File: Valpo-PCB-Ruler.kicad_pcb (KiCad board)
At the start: 2 copper layers, 159 x 38.1 mm, 40 parts, among them SW1 SW_Push, SW2 SW_Push, SW3 SW_Push, U2 USB_Board, U3 ATtiny85-20SU

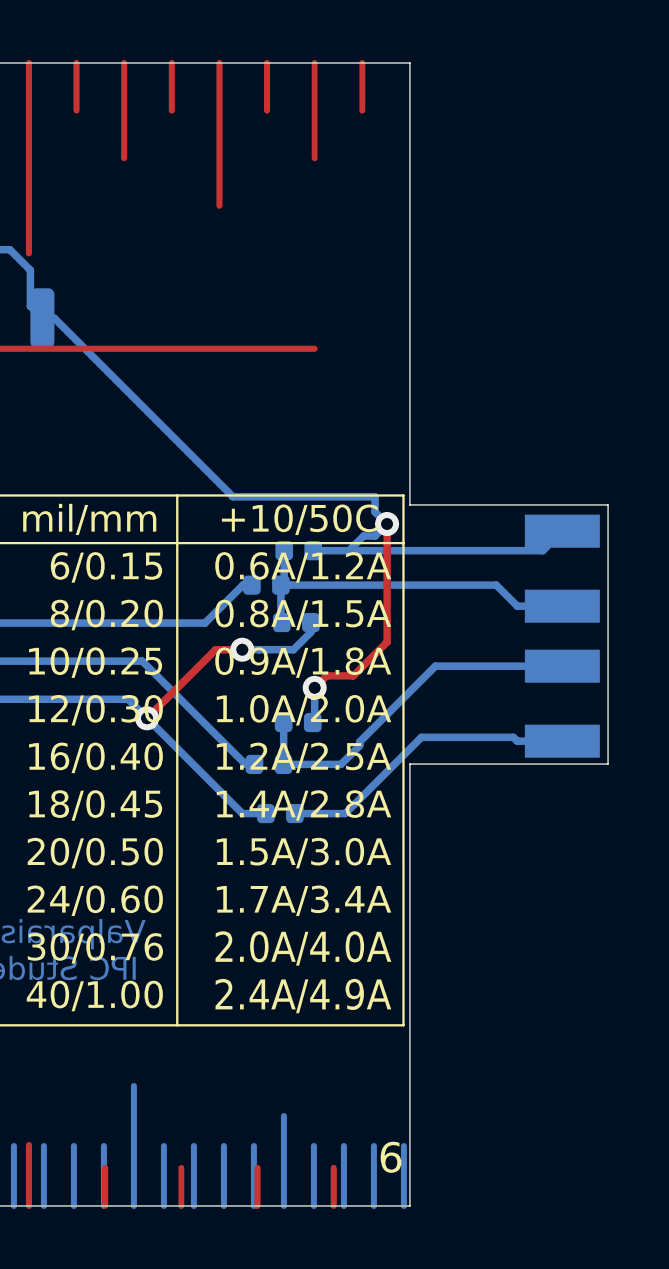
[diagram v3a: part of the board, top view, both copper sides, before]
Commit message: Reduce USB size
Brought the sides of the USB down to more closely fit the width of the pads.
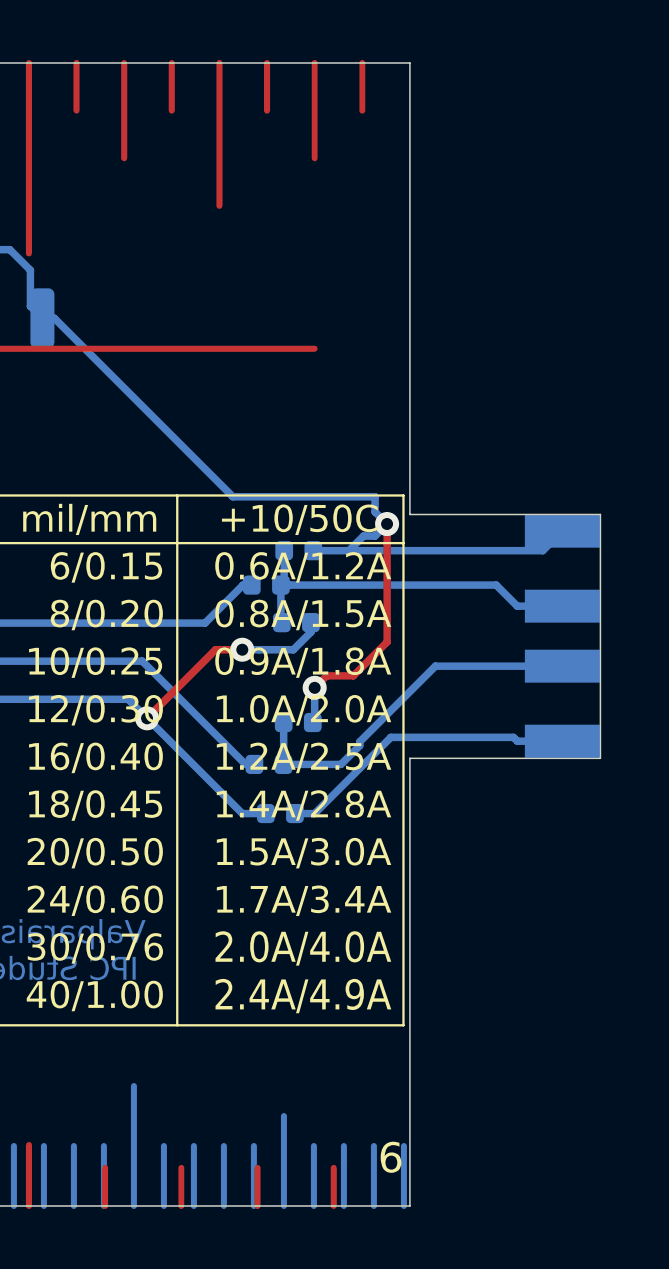
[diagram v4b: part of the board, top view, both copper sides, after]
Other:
- board size 159 x 38.1 mm -> 158.8 x 38.1 mm
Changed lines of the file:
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@@
     (tags diode)
     (attr smd)
-    (fp_text reference D2 (at 2.055 0) (layer B.SilkS)
+    (fp_text reference D2 (at -2.159 -0.254) (layer B.SilkS)
       (effects (font (size 1 1) (thickness 0.15)) (justify mirror))
     )
@@
     (effects (font (size 1 1) (thickness 0.15)) (justify left mirror))
   )
-  (gr_line (start 203.2 86.868) (end 209.804 86.868) (layer Edge.Cuts) (width 0.05))
-  (gr_line (start 203.2 78.232) (end 209.804 78.232) (layer Edge.Cuts) (width 0.05))
-  (gr_line (start 203.2 63.5) (end 203.2 78.232) (layer Edge.Cuts) (width 0.05))
-  (gr_line (start 209.804 78.232) (end 209.804 86.868) (layer Edge.Cuts) (width 0.05))
+  (gr_line (start 203.2 86.6775) (end 209.55 86.6775) (layer Edge.Cuts) (width 0.05))
+  (gr_line (start 203.2 78.5495) (end 209.55 78.5495) (layer Edge.Cuts) (width 0.05))
+  (gr_line (start 203.2 63.5) (end 203.2 78.5495) (layer Edge.Cuts) (width 0.05))
+  (gr_line (start 209.55 78.5495) (end 209.55 86.6775) (layer Edge.Cuts) (width 0.05))
   (gr_text -31 (at 90.3224 66.8147) (layer B.SilkS)
     (effects (font (size 0.75 0.75) (thickness 0.15)) (justify mirror))
@@
     (effects (font (size 3.048 3.048) (thickness 0.15)))
   )
-  (gr_line (start 203.2 86.868) (end 203.2 101.6) (layer Edge.Cuts) (width 0.05))
-  (via (at 197.612 83.058) (size 0.8) (drill 0.4) (layers F.Cu B.Cu) (net 2))
+  (gr_line (start 203.2 86.6775) (end 203.2 101.6) (layer Edge.Cuts) (width 0.05))
   (via (at 200.025 84.328) (size 0.8) (drill 0.4) (layers F.Cu B.Cu) (net 1))
   (segment (start 167.553 71.755) (end 167.953 71.755) (width 0.25) (layer B.Cu) (net 1))
@@
   (segment (start 167.953 71.755) (end 171.89 67.818) (width 0.25) (layer B.Cu) (net 1))
   (segment (start 171.89 67.818) (end 178.435 67.818) (width 0.25) (layer B.Cu) (net 1))
+  (via (at 197.612 83.058) (size 0.8) (drill 0.4) (layers F.Cu B.Cu) (net 2))
   (segment (start 198.177685 83.058) (end 197.612 83.058) (width 0.25) (layer B.Cu) (net 2))
   (segment (start 199.9003 82.4738) (end 199.3161 83.058) (width 0.25) (layer B.Cu) (net 2))
@@
   (segment (start 206.78 81.606) (end 206.0778 80.9038) (width 0.25) (layer B.Cu) (net 13))
   (segment (start 208.28 81.606) (end 206.78 81.606) (width 0.25) (layer B.Cu) (net 13))
-  (segment (start 206.78 86.106) (end 206.653 85.979) (width 0.25) (layer B.Cu) (net 14))
+  (segment (start 206.653 85.979) (end 202.565 85.979) (width 0.25) (layer B.Cu) (net 14))
+  (segment (start 200.025 88.519) (end 199.367 88.519) (width 0.25) (layer B.Cu) (net 14))
   (segment (start 208.28 86.106) (end 206.78 86.106) (width 0.25) (layer B.Cu) (net 14))
-  (segment (start 206.653 85.979) (end 203.581 85.979) (width 0.25) (layer B.Cu) (net 14))
-  (segment (start 201.041 88.519) (end 199.367 88.519) (width 0.25) (layer B.Cu) (net 14))
-  (segment (start 203.581 85.979) (end 201.041 88.519) (width 0.25) (layer B.Cu) (net 14))
+  (segment (start 202.565 85.979) (end 200.025 88.519) (width 0.25) (layer B.Cu) (net 14))
+  (segment (start 206.78 86.106) (end 206.653 85.979) (width 0.25) (layer B.Cu) (net 14))
 )
